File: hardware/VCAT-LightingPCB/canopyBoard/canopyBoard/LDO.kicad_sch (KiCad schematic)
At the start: 5 parts, among them U14 MCP1826S

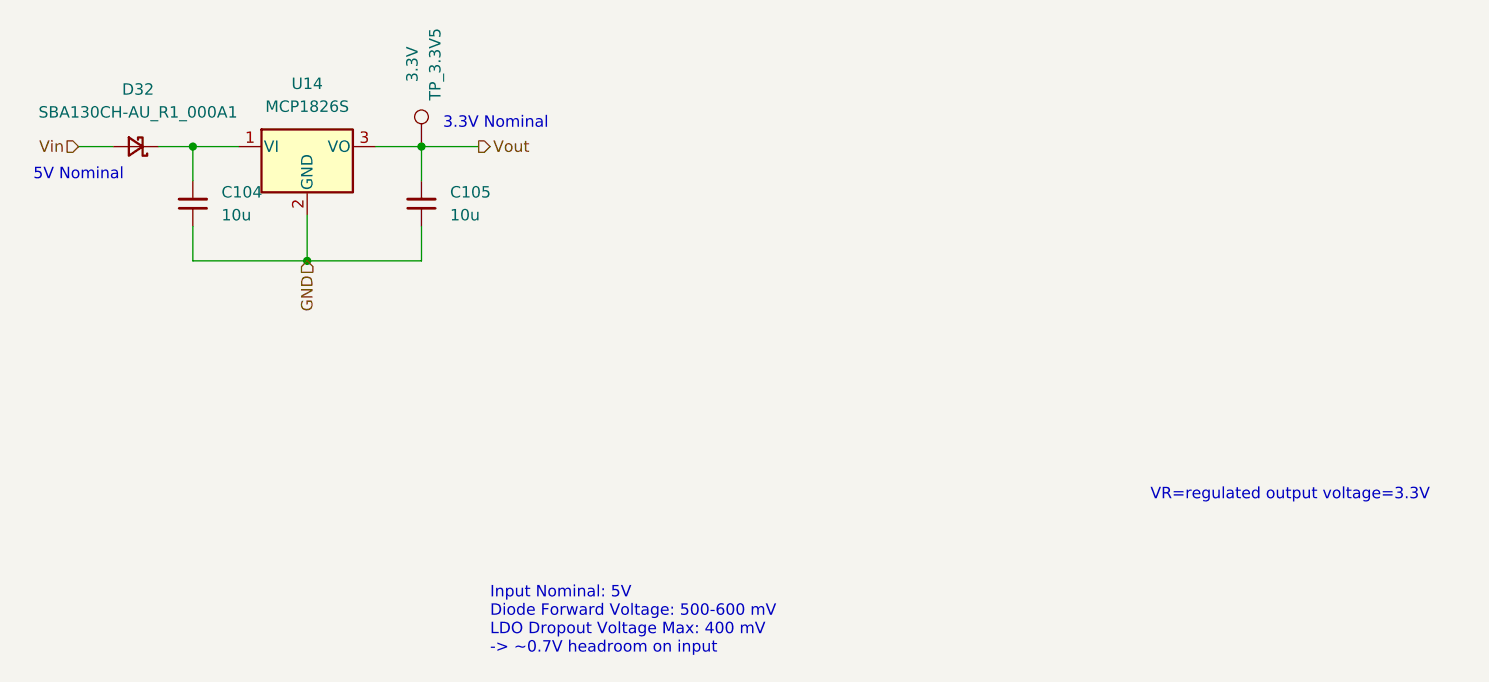
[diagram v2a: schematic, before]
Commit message: Untrack KiCad .history, convert KiCAD-Sharepoint to a submodule, remove LightsPCB
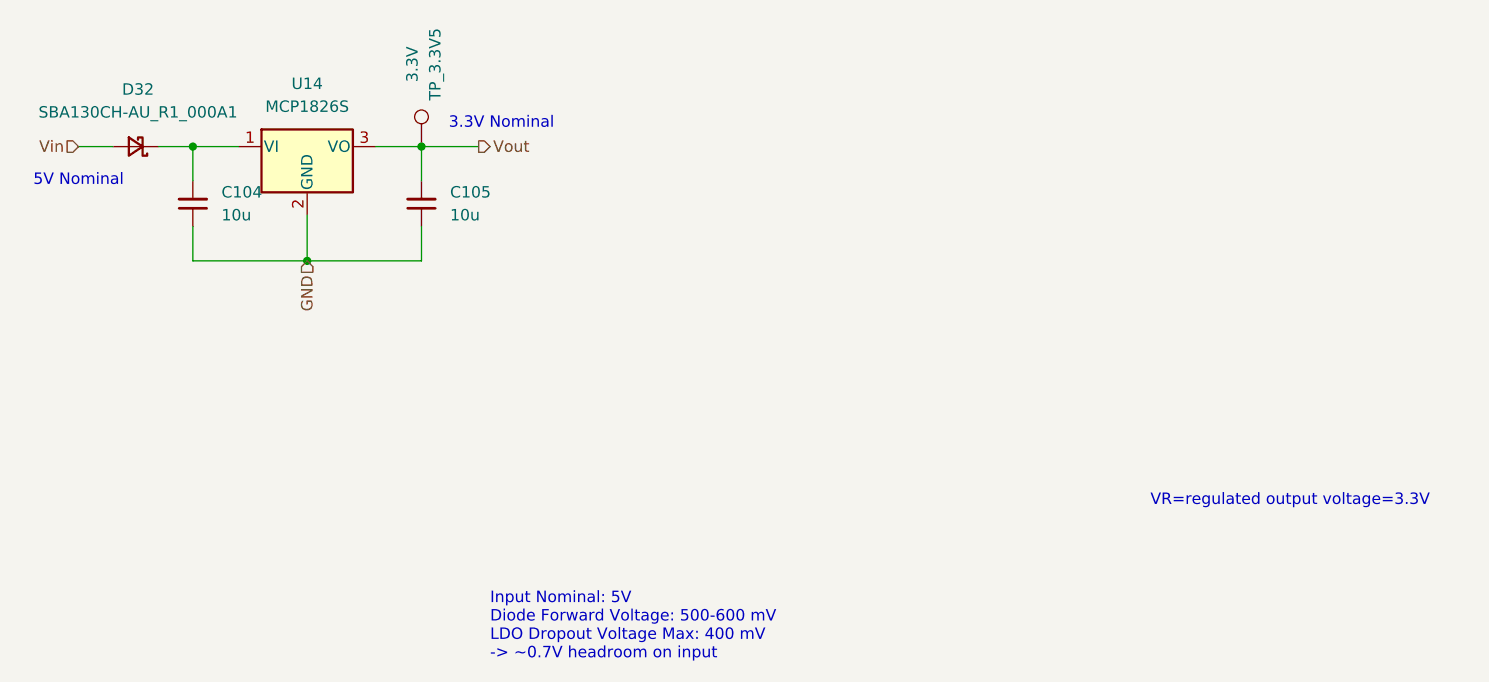
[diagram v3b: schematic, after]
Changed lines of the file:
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@@
 	(text "5V Nominal"
 		(exclude_from_sim no)
-		(at 127 66.675 0)
+		(at 127 67.31 0)
 		(effects
 			(font
@@
 	(text "Input Nominal: 5V\nDiode Forward Voltage: 500-600 mV\nLDO Dropout Voltage Max: 400 mV\n-> ~0.7V headroom on input"
 		(exclude_from_sim no)
-		(at 172.72 116.205 0)
+		(at 172.72 116.84 0)
 		(effects
 			(font
@@
 	(text "VR=regulated output voltage=3.3V"
 		(exclude_from_sim no)
-		(at 261.62 102.235 0)
+		(at 261.62 102.87 0)
 		(effects
 			(font
@@
 	(text "3.3V Nominal"
 		(exclude_from_sim no)
-		(at 173.355 60.96 0)
+		(at 173.99 60.96 0)
 		(effects
 			(font
